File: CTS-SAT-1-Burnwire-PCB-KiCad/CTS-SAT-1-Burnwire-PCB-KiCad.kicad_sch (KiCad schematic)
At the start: 16 parts, among them J1 feather long, J2 feather short, U1 ADP2303ARDZ

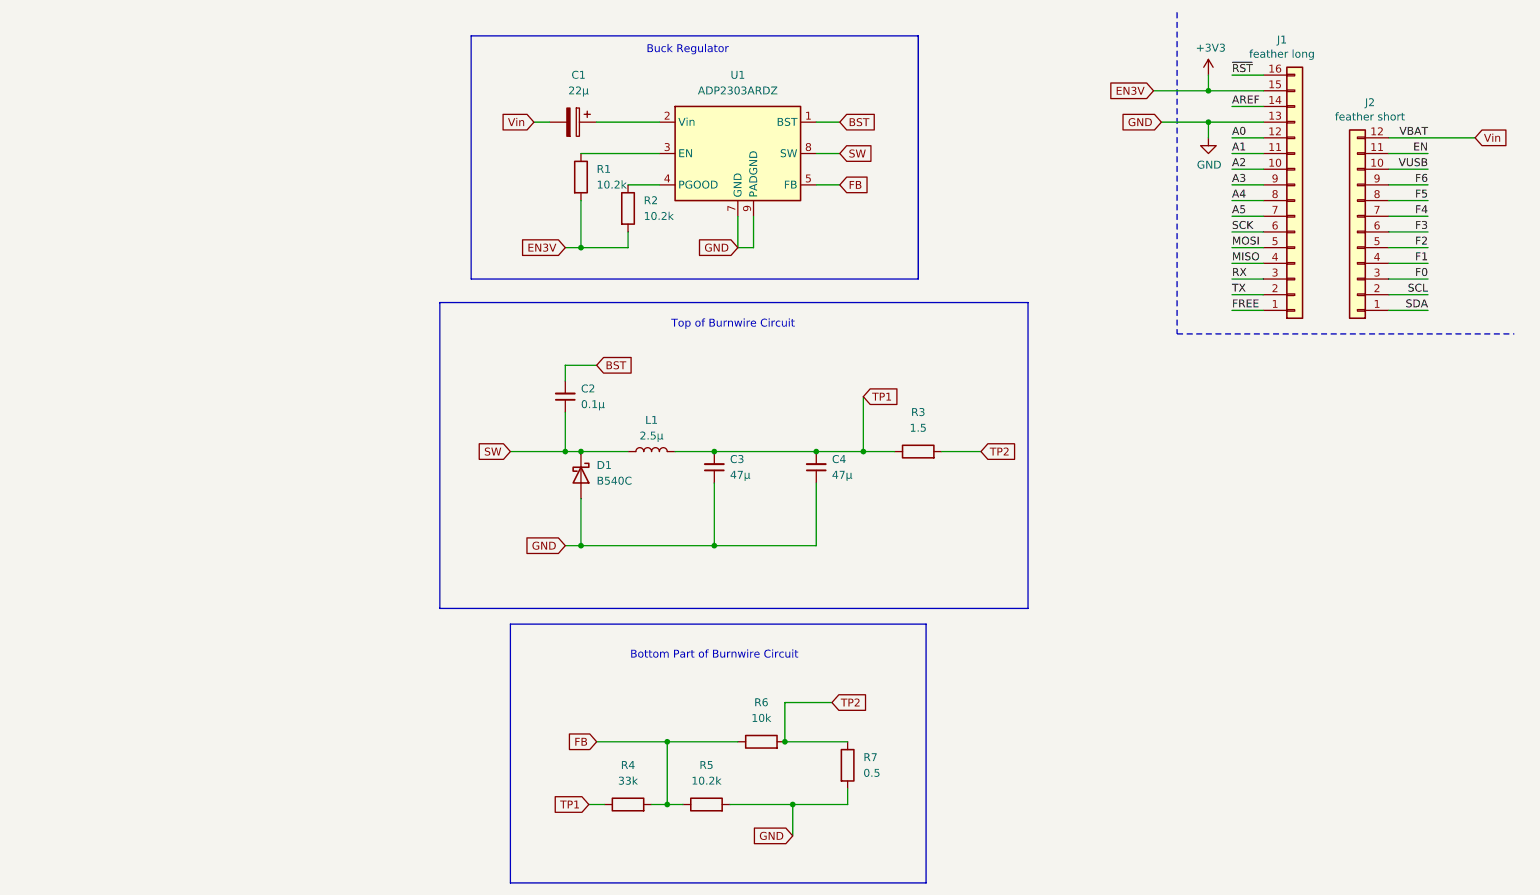
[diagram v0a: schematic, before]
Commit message: Organized Schematic and PCB Layout
Organized the Schematic to make it more neat and organized the ratsnest of the PCB.
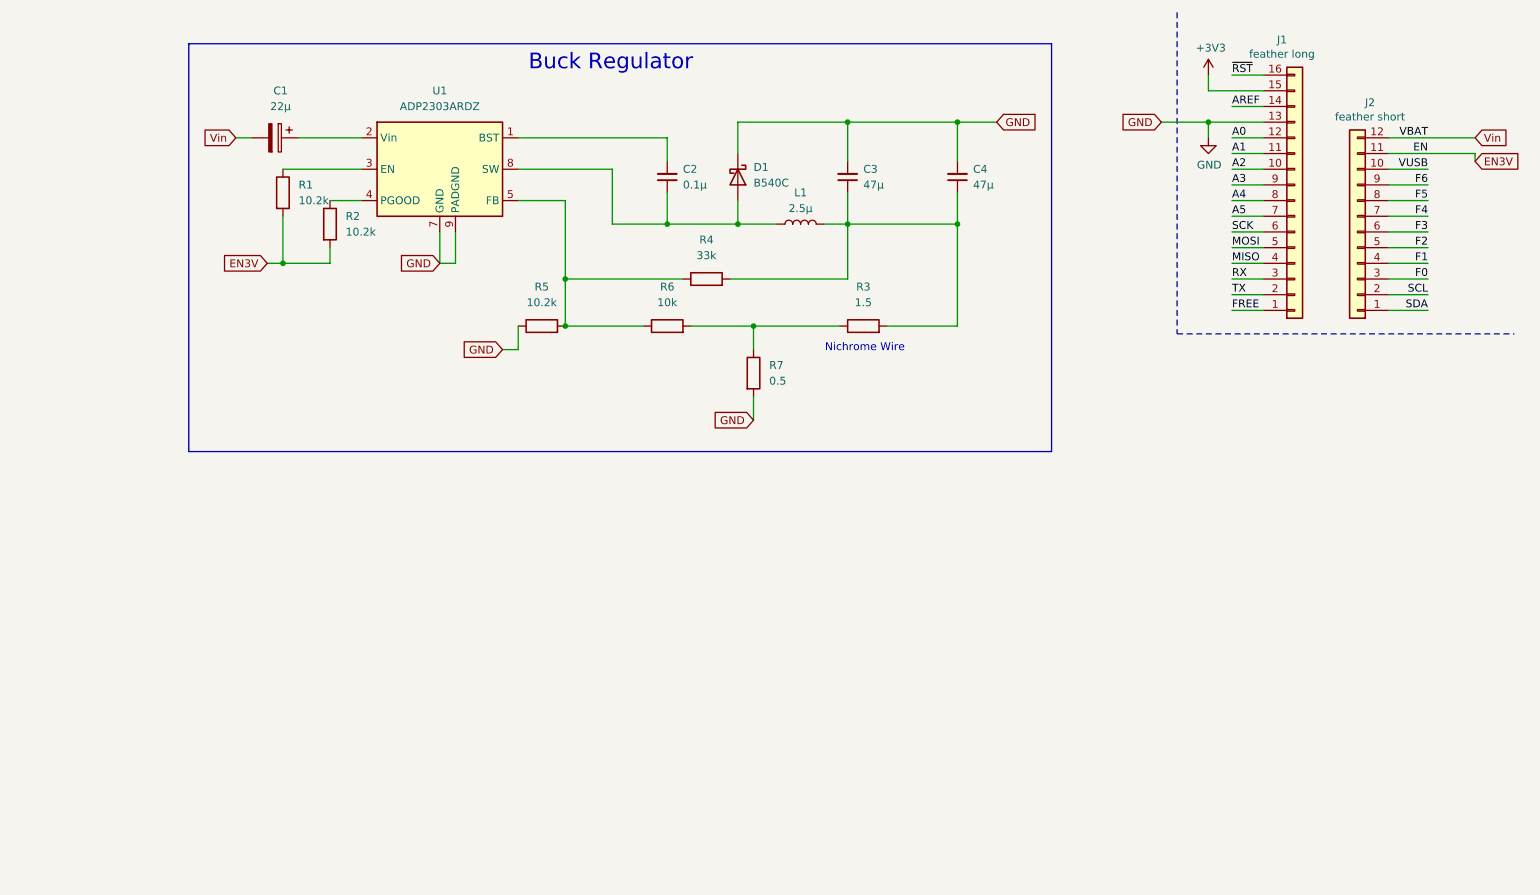
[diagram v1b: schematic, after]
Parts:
- C1: footprint (none) -> Capacitor_Tantalum_SMD:CP_EIA-1608-08_AVX-J
- C2, C3, C4: footprint (none) -> Capacitor_SMD:C_0201_0603Metric
- D1: footprint (none) -> Diode_SMD:D_01005_0402Metric
- L1: footprint (none) -> Inductor_SMD:L_0201_0603Metric
- R1, R2, R3, R4, R5, R6, R7: footprint (none) -> Resistor_SMD:R_0201_0603Metric
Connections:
- net +3V3: no longer R1.2, R2.2
- net GND: now also C3.2, C4.2, D1.1 (K), R5.1; no longer C3.1, C4.1, D1.2 (A), R5.2
- net BST: no longer names the net of C2.2, U1.1 (BST)
- net EN renamed EN3V
- net EN3V: now also R1.2, R2.2
- net FB: no longer names the net of R6.1, U1.5 (FB)
- net FB: now also R4.1, R5.2; no longer R4.2, R5.1
- net SW: no longer names the net of C2.1, L1.1, U1.8 (SW)
- net SW: now also D1.2 (A); no longer D1.1 (K)
- removed net TP1: C3.2, C4.2, L1.2, R3.1, R4.1
- net TP2: no longer names the net of R6.2, R7.1
- net TP2: now also R3.1; no longer R3.2
- new net: C3.1, C4.1, L1.2, R3.2, R4.2
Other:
- note added: "Nichrome Wire"
- note removed: "Bottom Part of Burnwire Circuit"
- note removed: "Top of Burnwire Circuit"
- moved on the sheet: C1, C2, C3, C4, D1, L1, R1, R2, R3, R4, R5, R6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

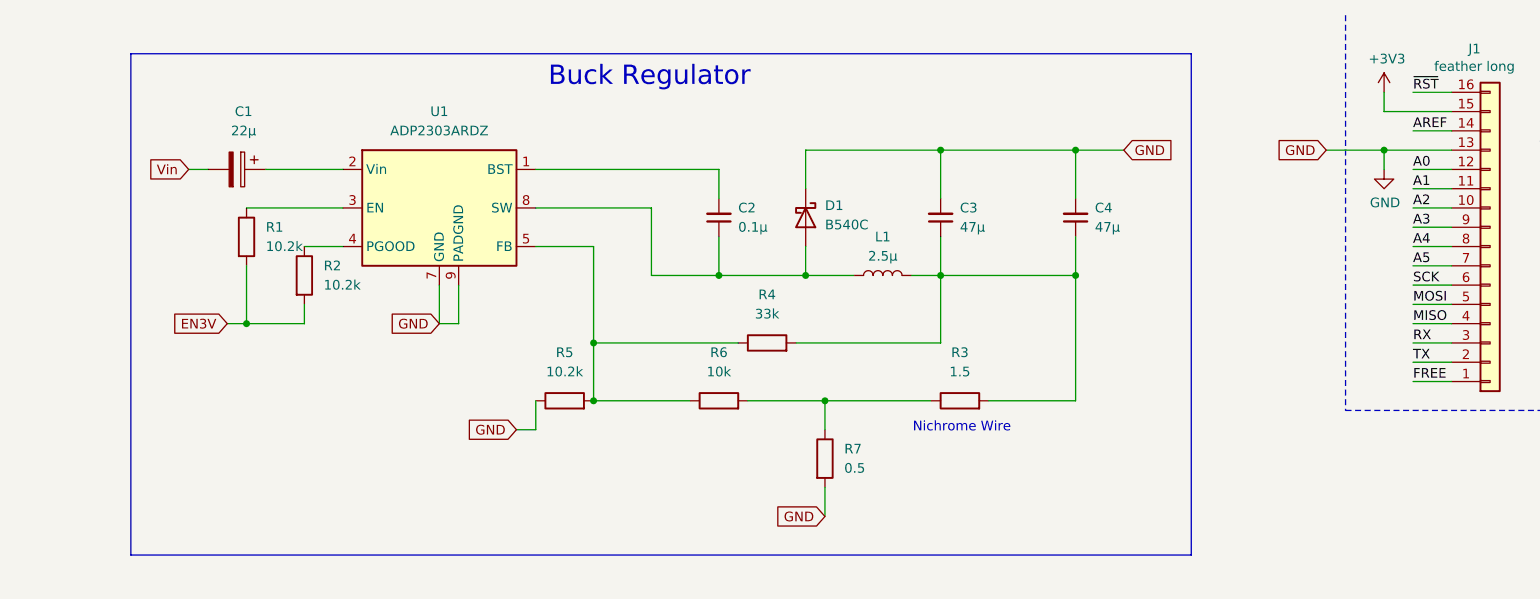
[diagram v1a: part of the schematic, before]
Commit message: Updated PCB design based on IC datasheet
Took out extra resistors and adjusted current value to output the right current through the burn resistor.
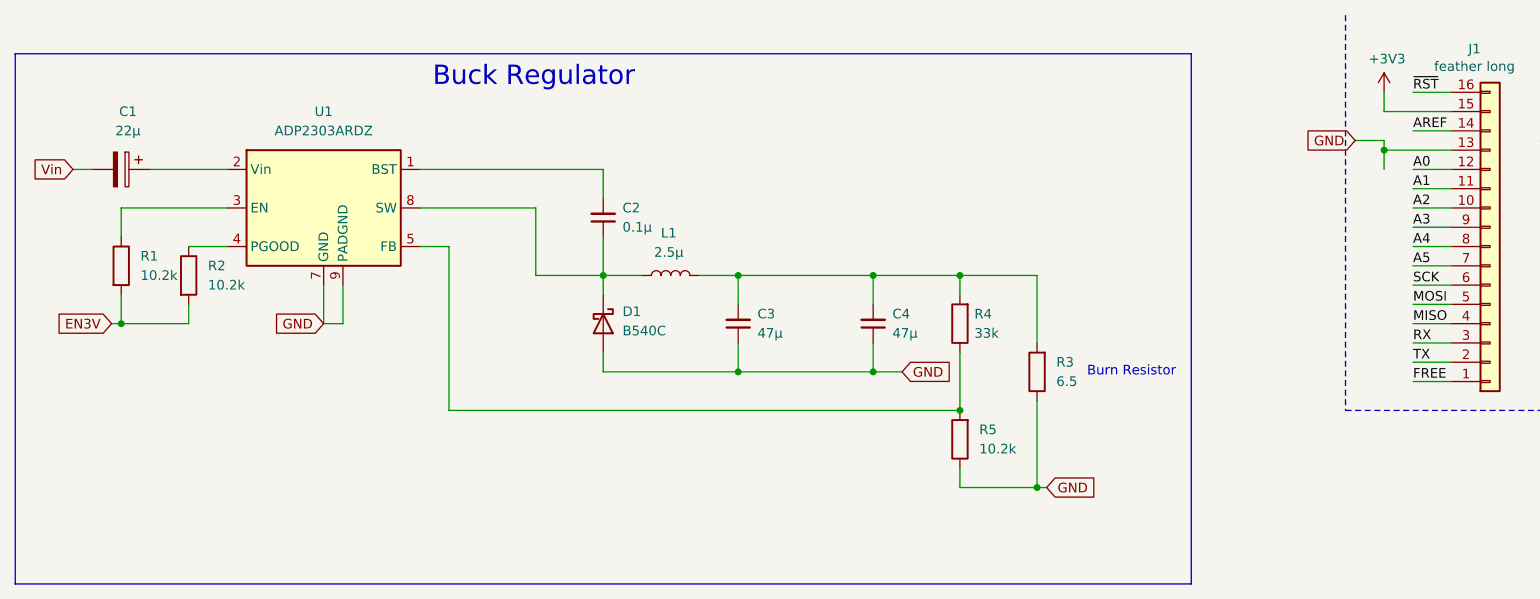
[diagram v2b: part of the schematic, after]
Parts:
- removed R6: 10k, Resistor_SMD:R_0201_0603Metric, symbol Device:R
- removed R7: 0.5, Resistor_SMD:R_0201_0603Metric, symbol Device:R
- R3: value 1.5 -> 6.5
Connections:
- net GND: now also C3.1, C4.1, D1.2 (A), R3.1; no longer C3.2, C4.2, D1.1 (K)
- net at L1.2, R3.2, R4.2: now also C3.2, C4.2; no longer C3.1, C4.1
- net at C2.1, L1.1, U1.8 (SW): now also D1.1 (K); no longer D1.2 (A)
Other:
- note added: "Burn Resistor"
- note removed: "Nichrome Wire"
- moved on the sheet: C1, C2, C3, C4, D1, L1, R1, R2, R3, R4, R5, U1

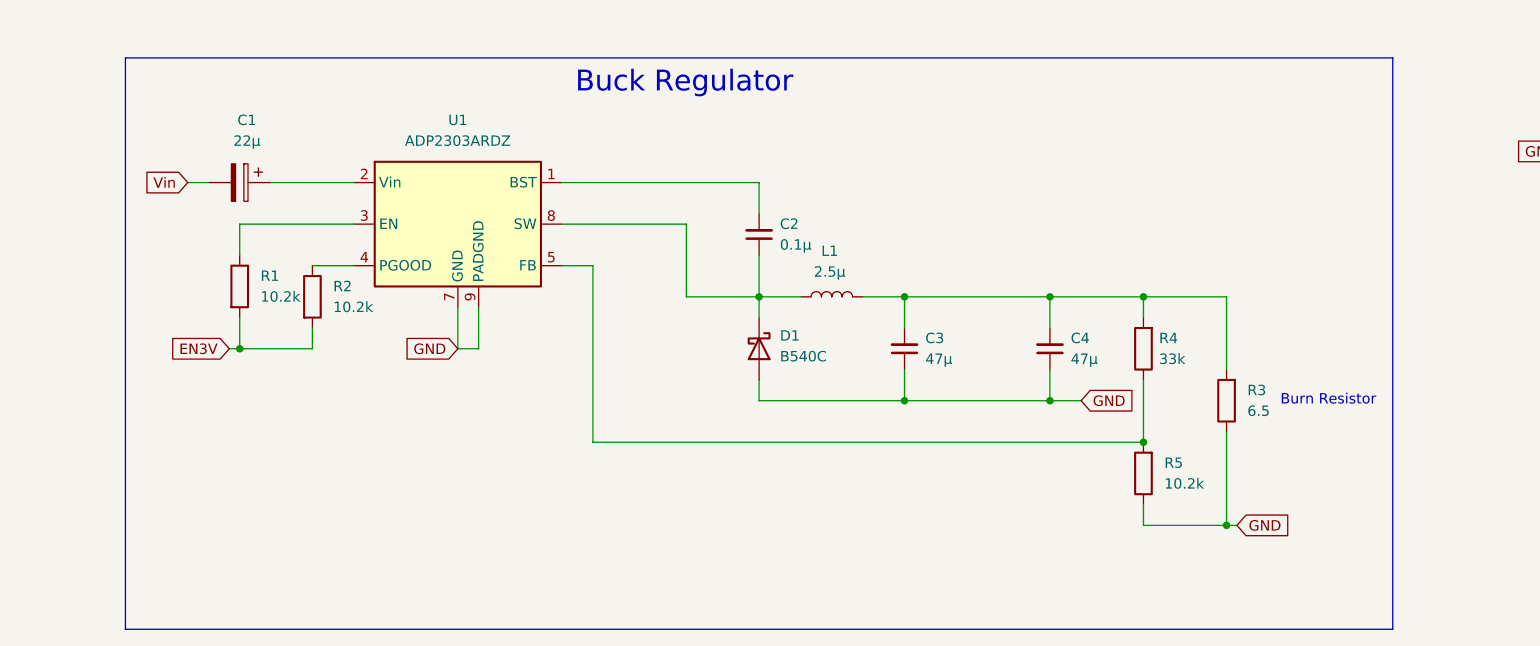
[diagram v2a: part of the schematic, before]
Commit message: Update CTS-SAT-1-Burnwire-PCB-KiCad.kicad_sch
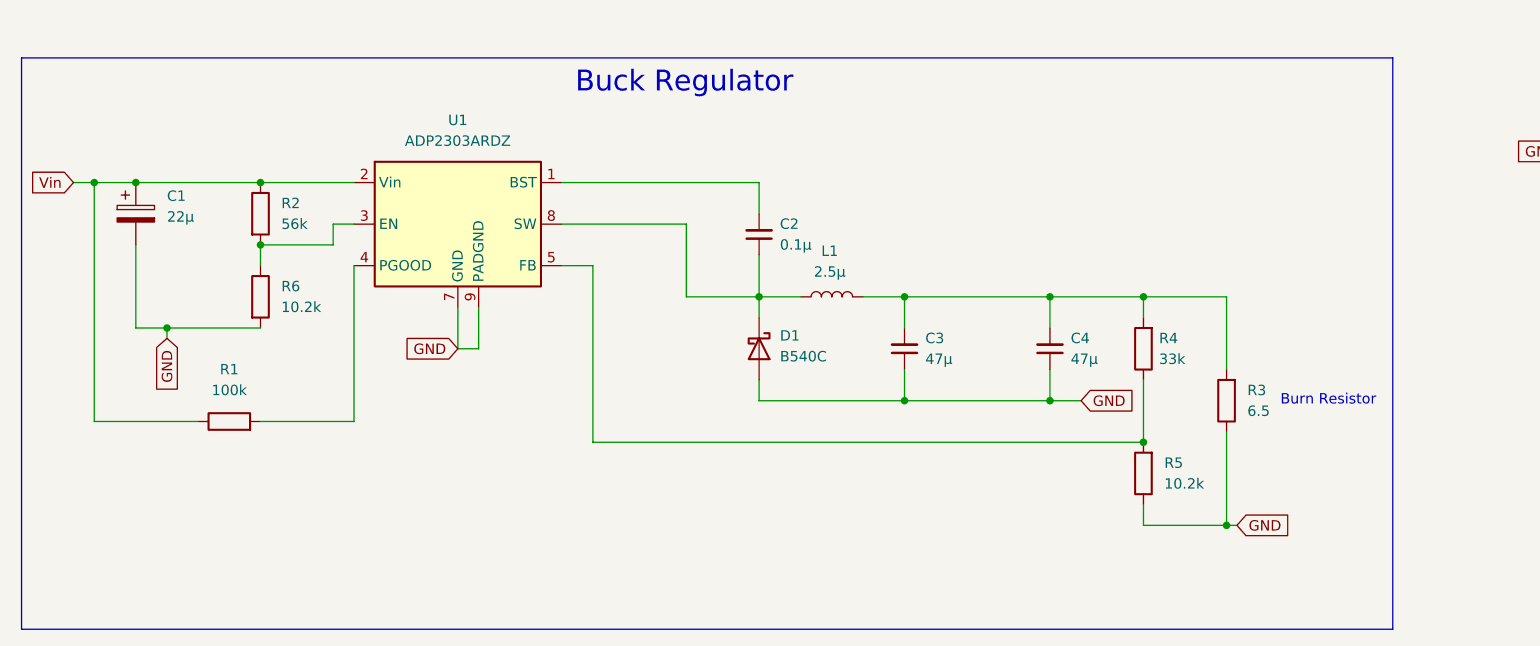
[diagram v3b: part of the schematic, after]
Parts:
- added R6: 10.2k, Resistor_SMD:R_0201_0603Metric, symbol Device:R
- R1: value 10.2k -> 100k
- R2: value 10.2k -> 56k
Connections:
- net EN3V: no longer R1.2, R2.2
- net GND: now also C1.2, R6.2
- net Vin: now also C1.1, R1.1, R2.1, U1.2 (Vin); no longer C1.2
- net at U1.3 (EN): now also R2.2, R6.1; no longer R1.1
- net at U1.4 (PGOOD): now also R1.2; no longer R2.1
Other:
- moved on the sheet: C1, R1, R2
